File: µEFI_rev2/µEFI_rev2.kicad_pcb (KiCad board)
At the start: 4 copper layers, 99.9 x 99.3 mm, 149 parts, among them J1 USB_B, J2 Tag connect, J3 36638-0002, Q1 ISL9V5045S3ST, Q2 ISL9V5045S3ST, Q3 ISL9V5045S3ST, Q4 ISL9V5045S3ST, Q5 2N3904, Q6 IRF540N, Q7 IRF540N, Q8 SS8050, Q9 SS8050, SW1 SW_Push, U1 MCZ33810EK, U10 SensorsV2, U11 SensorsV2, U12 SensorsV2, U13 SensorsV2, U14 SensorsV2, U2 SensorsV2, U20 TPL7407LAPWR, U22 TPL7407LAPWR, U23 PaP_Driver_v1, U27 LM321, U3 STM32F407VGTx, U31 LM321, U36 MAX9926UAEE+, U4 MIC2940A-3.3WU, U5 MIC2940A-5.0WT, U6 LT4363IMS, U7 25LCxxx, U8 SensorsV2, U9 SensorsV2, Y1 25MHz

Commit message: uEFI v2 beta release
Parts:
- added C34: 4.7nF, Capacitor_SMD:C_0805_2012Metric, F.Cu at (125.2, 97.9)
- added H1: MountingHole, MountingHole:MountingHole_2.2mm_M2_Pad_Via, F.Cu at (99.9, 141.1)
- added H2: MountingHole, MountingHole:MountingHole_2.2mm_M2_Pad_Via, F.Cu at (188.9, 59.3)
- added H3: MountingHole, MountingHole:MountingHole_2.2mm_M2_Pad_Via, F.Cu at (130.3, 74.0)
- added H4: MountingHole, MountingHole:MountingHole_2.2mm_M2_Pad_Via, F.Cu at (186.9, 141.7)
- added H5: MountingHole, TestPoint:TestPoint_Pad_D1.0mm, F.Cu at (95.6, 145.0)
- added H6: MountingHole, TestPoint:TestPoint_Pad_D1.0mm, F.Cu at (190.1, 53.1)
- added H7: MountingHole, TestPoint:TestPoint_Pad_D1.0mm, F.Cu at (99.6, 53.0)
- added H8: MountingHole, TestPoint:TestPoint_Pad_D1.0mm, F.Cu at (158.7, 131.2)
- added Q10: IRF540N, Package_TO_SOT_THT:TO-220-3_Vertical, F.Cu at (183.0, 99.0)
- added R1: R_Small, Resistor_SMD:R_1206_3216Metric, F.Cu at (118.9, 98.3)
- added R28: R_Small, Resistor_SMD:R_1206_3216Metric, F.Cu at (121.4, 98.3)
- added R33: 10R 1/10W, Resistor_SMD:R_0603_1608Metric, B.Cu at (180.8, 100.1)
- added TP3: TestPoint, TestPoint:TestPoint_Pad_1.0x1.0mm, B.Cu at (126.2, 62.2)
- added TP4: TestPoint, TestPoint:TestPoint_Pad_1.0x1.0mm, B.Cu at (122.3, 82.8)
- added TP5: TestPoint, TestPoint:TestPoint_Pad_1.0x1.0mm, B.Cu at (120.2, 82.8)
- added TP6: TestPoint, TestPoint:TestPoint_Pad_1.0x1.0mm, B.Cu at (116.8, 64.8)
- added TP7: TestPoint, TestPoint:TestPoint_Pad_1.0x1.0mm, B.Cu at (120.4, 86.2)
- added TP8: TestPoint, TestPoint:TestPoint_Pad_1.0x1.0mm, B.Cu at (120.4, 89.6)
- added U15: TJA1042T3118, Package_SO:HTSOP-8-1EP_3.9x4.9mm_P1.27mm_EP2.4x3.2mm, F.Cu at (120.0, 105.2)
- C10, C11, C13, C15, C16, C19, C2, C21, C24, C26, C3, C5, C6, R10, R12, R14, R16: moved to B.Cu
- D2, D3: footprint Diode_SMD:D_0805_2012Metric -> Diode_SMD:D_SOD-523
- Q5: value 2N3904 -> SS8050; footprint Package_TO_SOT_SMD:TSOT-23 -> Package_TO_SOT_SMD:SOT-23
- moved JP11 164.7 mm to (175.9, 127.3)
- moved D14 162.6 mm to (174.8, 123.0)
- moved R82 158.7 mm to (171.0, 122.2), turned to 90 degrees
- moved C51 156.8 mm to (167.7, 126.7), turned to -90 degrees
- moved U27 154.3 mm to (172.1, 126.7)
- moved R83 152.9 mm to (167.7, 122.6), turned to 90 degrees
- moved C16 137.7 mm to (188.6, 117.0)
- moved R2 116.3 mm to (130.0, 118.6), turned to 90 degrees
- moved J2 105.9 mm to (142.8, 132.8), turned to 45 degrees
- moved TP1 99.0 mm to (128.5, 121.4)
- moved C11 97.2 mm to (123.0, 125.9), turned to -90 degrees
- moved C6 96.3 mm to (121.6, 143.8), turned to -45 degrees
- moved C12 92.6 mm to (137.2, 131.9), turned to 0 degrees
- moved C13 89.3 mm to (118.3, 131.7)
- moved C5 87.2 mm to (111.6, 136.4), turned to -135 degrees
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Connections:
- C18 pad 1: CONN_62 -> M1
- C19 pad 1: CONN_42 -> M2
- C20 pad 1: CONN_61 -> L1
- C21 pad 1: CONN_41 -> L2
- C23 pad 1: CONN_61 -> L1
- C24 pad 1: CONN_41 -> L2
- C25 pad 1: CONN_62 -> M1
- C26 pad 1: CONN_42 -> M2
- C27 pad 2: CONN_22 -> L4
- C28 pad 2: CONN_2 -> L3
- C29 pad 2: CONN_1 -> M4
- C30 pad 2: CONN_21 -> M3
- C49 pad 1: CONN_17 -> B1
- C52 pad 1: CONN_68 -> CMP-
- C53 pad 1: CONN_69 -> CMP+
- C55 pad 1: CONN71+ -> CKP+
- C56 pad 1: CONN71- -> CKP-
- J1 pad 1: unconnected-(J1-Pad1) -> /VBUS
- J1 pad 4: GND1 -> GND
- J1 pad 5: GND1 -> GND
- J3 pad A1: unconnected-(J3-PadA1) -> A1
- J3 pad A2: unconnected-(J3-PadA2) -> A2
- J3 pad A3: unconnected-(J3-PadA3) -> A3
- J3 pad A4: unconnected-(J3-PadA4) -> +12VA
- J3 pad B1: unconnected-(J3-PadB1) -> B1
- J3 pad B2: unconnected-(J3-PadB2) -> B2
- J3 pad B3: unconnected-(J3-PadB3) -> B3
- J3 pad B4: unconnected-(J3-PadB4) -> B4
- J3 pad C1: unconnected-(J3-PadC1) -> C1
- J3 pad C2: unconnected-(J3-PadC2) -> C2
- J3 pad C3: unconnected-(J3-PadC3) -> C3
- J3 pad C4: unconnected-(J3-PadC4) -> C4
- J3 pad D1: unconnected-(J3-PadD1) -> D1
- J3 pad D2: unconnected-(J3-PadD2) -> D2
- J3 pad D3: unconnected-(J3-PadD3) -> D3
- J3 pad D4: unconnected-(J3-PadD4) -> D4
- J3 pad E1: unconnected-(J3-PadE1) -> E1
- J3 pad E2: unconnected-(J3-PadE2) -> E2
- J3 pad E3: unconnected-(J3-PadE3) -> E3
- J3 pad E4: unconnected-(J3-PadE4) -> E4
- J3 pad F1: unconnected-(J3-PadF1) -> F1
- J3 pad F2: unconnected-(J3-PadF2) -> F2
- J3 pad F3: unconnected-(J3-PadF3) -> F3
- J3 pad F4: unconnected-(J3-PadF4) -> F4
- J3 pad G1: unconnected-(J3-PadG1) -> G1
- J3 pad G2: unconnected-(J3-PadG2) -> G2
- J3 pad G3: unconnected-(J3-PadG3) -> G3
- J3 pad G4: unconnected-(J3-PadG4) -> G4
- J3 pad H1: unconnected-(J3-PadH1) -> H1
- J3 pad H2: unconnected-(J3-PadH2) -> H2
- J3 pad H3: unconnected-(J3-PadH3) -> H3
- J3 pad H4: unconnected-(J3-PadH4) -> H4
- J3 pad J1: unconnected-(J3-PadJ1) -> J1
- J3 pad J2: unconnected-(J3-PadJ2) -> CAN+
- J3 pad J3: unconnected-(J3-PadJ3) -> CMP-
- J3 pad J4: unconnected-(J3-PadJ4) -> CKP-
- J3 pad K1: unconnected-(J3-PadK1) -> K1
- J3 pad K2: unconnected-(J3-PadK2) -> CAN-
- J3 pad K3: unconnected-(J3-PadK3) -> CMP+
- J3 pad K4: unconnected-(J3-PadK4) -> CKP+
- J3 pad L1: unconnected-(J3-PadL1) -> L1
- J3 pad L2: unconnected-(J3-PadL2) -> L2
- J3 pad L3: unconnected-(J3-PadL3) -> L3
- J3 pad L4: unconnected-(J3-PadL4) -> L4
- J3 pad M1: unconnected-(J3-PadM1) -> M1
- J3 pad M2: unconnected-(J3-PadM2) -> M2
- J3 pad M3: unconnected-(J3-PadM3) -> M3
- J3 pad M4: unconnected-(J3-PadM4) -> M4
- Q1 pad 2: CONN_42 -> M2
- Q2 pad 2: CONN_62 -> M1
- Q3 pad 2: CONN_61 -> L1
- Q4 pad 2: CONN_41 -> L2
- Q5 pad 1: +12VA -> Net-(D2-Pad1)
- Q5 pad 2: Net-(D2-Pad1) -> +12VA
- R112 pad 1: CONN_68 -> CMP-
- R116 pad 1: CONN71- -> CKP-
- R117 pad 1: CONN71+ -> CKP+
- R13 pad 2: CONN_62 -> M1
- R14 pad 2: CONN_42 -> M2
- R15 pad 2: CONN_61 -> L1
- R16 pad 2: CONN_41 -> L2
- R24 pad 2: /CAN_RX -> /LED_CAN_RX
- R5 pad 2: /CAN_TX -> /LED_CAN_TX
- R81 pad 1: CONN_69 -> CMP+
- R87 pad 1: CONN_17 -> B1
- R92 pad 1: CONN_17 -> B1
- R97 pad 2: CONN_17 -> B1
- U1 pad 1: CONN_21 -> M3
- U1 pad 16: CONN_1 -> M4
- U1 pad 17: CONN_22 -> L4
- U1 pad 32: CONN_2 -> L3
- U10 pad 1: unconnected-(U10-Pad1) -> +5VA
- U10 pad 2: unconnected-(U10-Pad2) -> +12V
- U10 pad 3: unconnected-(U10-Pad3) -> J1
- U10 pad 4: unconnected-(U10-Pad4) -> /Sensores/PA3
- U10 pad 5: unconnected-(U10-Pad5) -> GND
- U11 pad 1: unconnected-(U11-Pad1) -> +5VA
- U11 pad 2: unconnected-(U11-Pad2) -> +12V
- U11 pad 3: unconnected-(U11-Pad3) -> D1
- U11 pad 4: unconnected-(U11-Pad4) -> /Sensores/PA4
- U11 pad 5: unconnected-(U11-Pad5) -> GND
- U12 pad 1: unconnected-(U12-Pad1) -> +5VA
- U12 pad 2: unconnected-(U12-Pad2) -> +12V
- U12 pad 3: unconnected-(U12-Pad3) -> F1
- U12 pad 4: unconnected-(U12-Pad4) -> /Sensores/PA5
- U12 pad 5: unconnected-(U12-Pad5) -> GND
- U13 pad 1: unconnected-(U13-Pad1) -> +5VA
- U13 pad 2: unconnected-(U13-Pad2) -> +12V
- U13 pad 3: unconnected-(U13-Pad3) -> C1
- U13 pad 4: unconnected-(U13-Pad4) -> /Sensores/PA6
- U13 pad 5: unconnected-(U13-Pad5) -> GND
- U14 pad 1: unconnected-(U14-Pad1) -> +5VA
- U14 pad 2: unconnected-(U14-Pad2) -> +12V
- U14 pad 3: unconnected-(U14-Pad3) -> G1
- U14 pad 4: unconnected-(U14-Pad4) -> /Sensores/PA7
- U14 pad 5: unconnected-(U14-Pad5) -> GND
- U2 pad 1: unconnected-(U2-Pad1) -> +5VA
- U2 pad 2: unconnected-(U2-Pad2) -> +12V
- U2 pad 3: unconnected-(U2-Pad3) -> K1
- U2 pad 4: unconnected-(U2-Pad4) -> /Sensores/PA0
- U2 pad 5: unconnected-(U2-Pad5) -> GND
- U20 pad 10: CONN_58 -> D3
- U20 pad 11: CONN_18 -> E3
- U20 pad 12: CONN_39 -> B4
- U20 pad 13: CONN_39 -> B4
- U20 pad 14: CONN_40 -> C4
- U20 pad 15: CONN_40 -> C4
- U20 pad 16: CONN_40 -> C4
- U22 pad 10: CONN_63 -> F3
- U22 pad 11: CONN_64 -> D4
- U22 pad 12: CONN_64 -> D4
- U22 pad 13: CONN_65 -> G3
- U22 pad 14: CONN_65 -> G3
- U22 pad 15: CONN_66 -> H3
- U22 pad 16: CONN_66 -> H3
- U22 pad 7: /PWM/Relays/R3 -> /R_LMB
- U23 pad 11: CONN_75 -> H4
- U23 pad 12: CONN_76 -> G4
- U23 pad 13: CONN_77 -> F4
- U23 pad 14: CONN_78 -> E4
- U3 pad 15: unconnected-(U3-Pad15) -> 5V_ENABLE
- U8 pad 1: unconnected-(U8-Pad1) -> +5VA
- U8 pad 2: unconnected-(U8-Pad2) -> +12V
- U8 pad 3: unconnected-(U8-Pad3) -> E1
- U8 pad 4: unconnected-(U8-Pad4) -> /Sensores/PA1
- U8 pad 5: unconnected-(U8-Pad5) -> GND
- U9 pad 1: unconnected-(U9-Pad1) -> +5VA
- U9 pad 2: unconnected-(U9-Pad2) -> +12V
- U9 pad 3: unconnected-(U9-Pad3) -> H1
- U9 pad 4: unconnected-(U9-Pad4) -> /Sensores/PA2
- U9 pad 5: unconnected-(U9-Pad5) -> GND
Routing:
- net +3V3: track 0.00 -> 265.6 mm, vias 0 -> 15
- net +12V: track 0.00 -> 253.3 mm, vias 1 -> 4
- net GND: track 17.4 -> 191.6 mm, vias 11 -> 53
- net /MIL_OUT: track 0.00 -> 170.0 mm, vias 0 -> 6
- net /CHK_OUT: track 0.00 -> 164.2 mm, vias 0 -> 4
- net +5VA: track 15.5 -> 127.5 mm, vias 3 -> 4
- net /VBUS: track 0.00 -> 104.3 mm, vias 0 -> 2
- net /Sensores/PA7: track 0.00 -> 98.2 mm, vias 0 -> 2
- net /TIM9_CH2: track 0.00 -> 97.2 mm, vias 0 -> 2
- net /TIM9_CH1: track 0.00 -> 96.5 mm, vias 0 -> 2
- net 5V_ENABLE: track 0.00 -> 94.6 mm, vias 0 -> 2
- net /Sensores/PA6: track 0.00 -> 94.0 mm, vias 0 -> 1
- net /MTR_ENABLE: track 0.00 -> 89.8 mm, vias 0 -> 1
- net /R_LMB: track 0.00 -> 89.5 mm, vias 0 -> 2
- net /Sensores/PA3: track 0.00 -> 87.3 mm, vias 0 -> 1
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- added copper zone on B.Cu, net +3V3
- added copper zone on F.Cu, net +3V3
- added copper zone on B.Cu, net GND
- added copper zone on F.Cu, net GND
- added copper zone on In2.Cu, net GND
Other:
- board text added: "Aca podria ir otro soporte, pero de plastico, tipo trabita"
- board text added: "Aca va a ir un header con todos los pines que esten al pedo y sirvan para hacer de expansora"
- board text added: "Alimentacion sensores:"
- board text added: "Battery"
- board text added: "EN"
- board text added: "Faltan los caps elec[..] para filtrar el ruido, tambien ceramicos / tantalio"
- board text added: "Flash"
- board text added: "O2 Sensor"
- board text added: "PaP Driver"
- board text added: "RESET"
- board text added: "Salida tacometro"
- board text removed: "GNC_IN"
- board text removed: "O2 Sensor (A)"
- board text removed: "RPM_OUT"
- board text removed: "RSP ?"
- board text removed: "can"
- board text removed: "ckp"
- board text removed: "cmp"

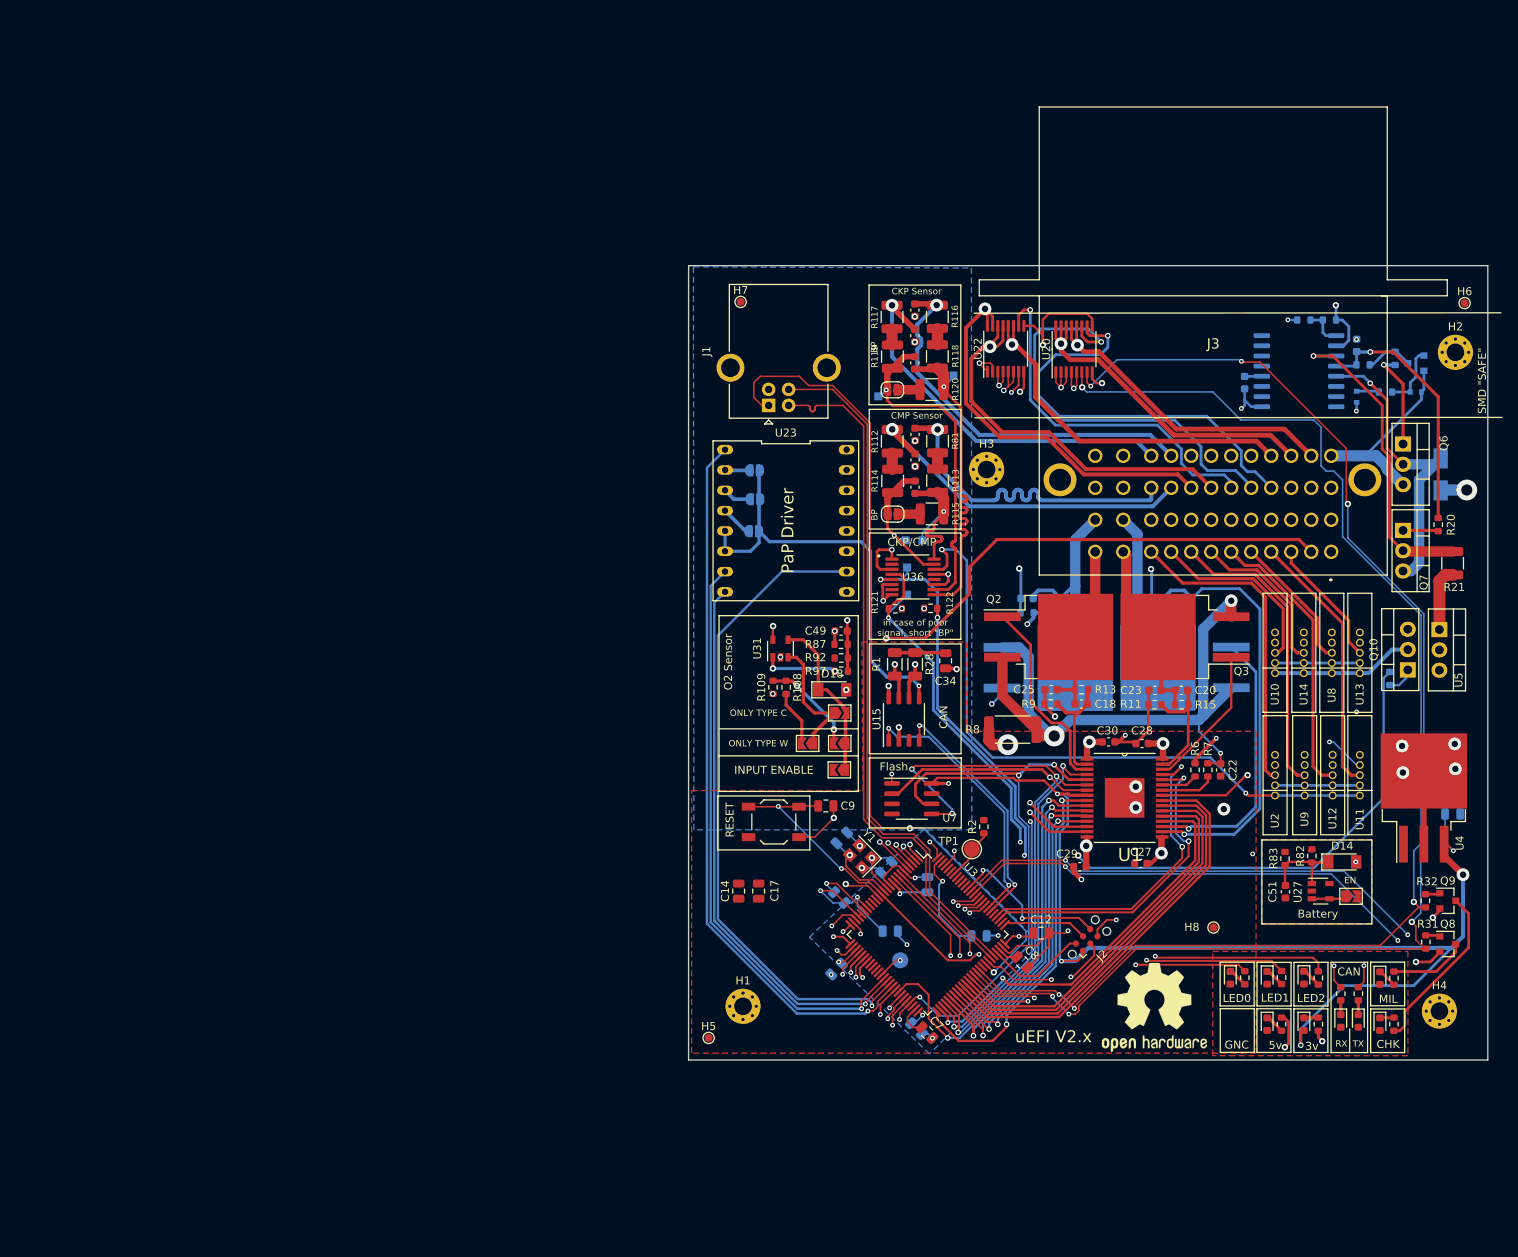
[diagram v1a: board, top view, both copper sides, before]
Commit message: bump to kicad 6, init uEFI v3
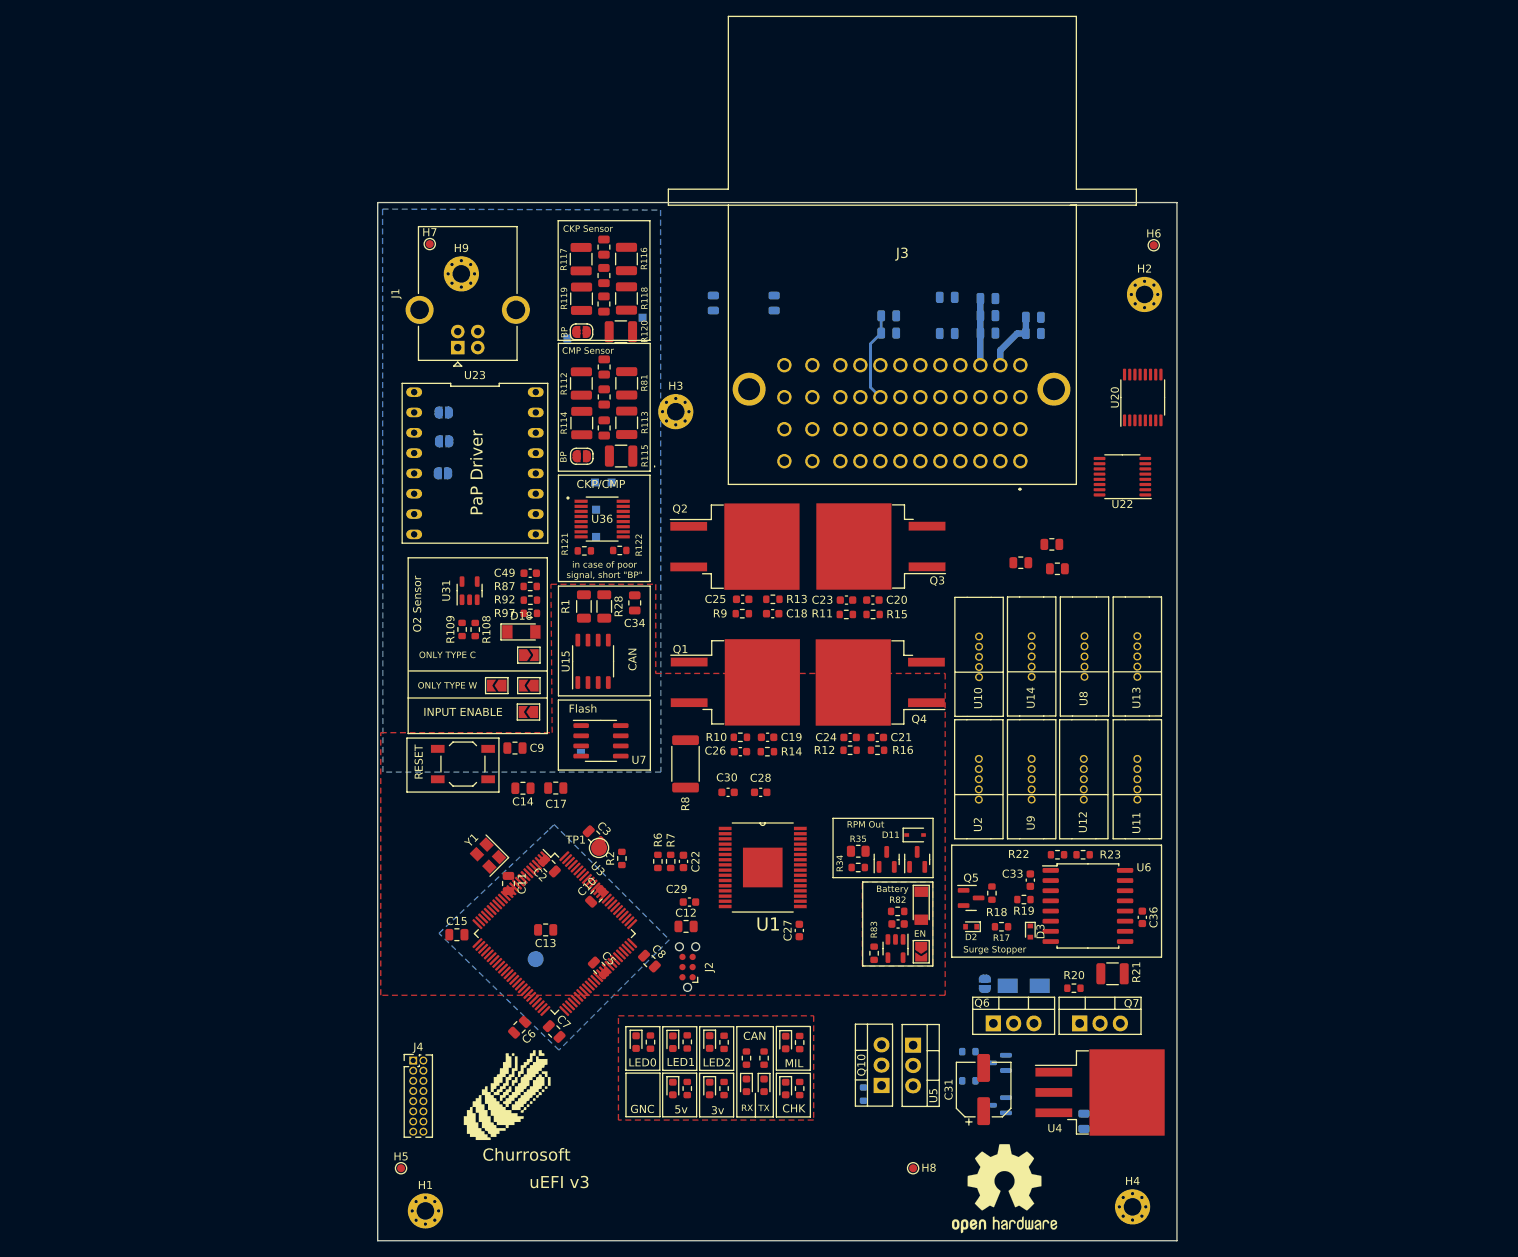
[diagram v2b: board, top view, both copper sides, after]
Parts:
- added C31: 100uF ±20% 35V, Capacitor_SMD:CP_Elec_6.3x7.7, F.Cu at (130.0, 151.5)
- added Churrosoft: SYM_Hot_Large, OpenEFI-STM32F_rev3:churro_new_v4, F.Cu at (70.6, 152.1)
- added D11: MM3Z24VT1G, Diode_SMD:D_SOD-323, F.Cu at (121.4, 119.6)
- added F1: 750mA, Fuse:Fuse_0805_2012Metric, B.Cu at (118.1, 54.7)
- added F10: 750mA, Fuse:Fuse_0805_2012Metric, B.Cu at (136.2, 54.9)
- added F11: 750mA, Fuse:Fuse_0805_2012Metric, B.Cu at (136.2, 56.9)
- added F12: 750mA, Fuse:Fuse_0805_2012Metric, F.Cu at (134.6, 85.6)
- added F13: 750mA, Fuse:Fuse_0805_2012Metric, B.Cu at (125.4, 52.4)
- added F14: 750mA, Fuse:Fuse_0805_2012Metric, B.Cu at (125.4, 56.9)
- added F2: 750mA, Fuse:Fuse_0805_2012Metric, F.Cu at (139.2, 86.4)
- added F3: 750mA, Fuse:Fuse_0805_2012Metric, B.Cu at (118.1, 56.9)
- added F4: 750mA, Fuse:Fuse_0805_2012Metric, B.Cu at (103.8, 53.1)
- added F5: 750mA, Fuse:Fuse_0805_2012Metric, B.Cu at (130.5, 56.9)
- added F6: 750mA, Fuse:Fuse_0805_2012Metric, B.Cu at (96.2, 53.1)
- added F7: 750mA, Fuse:Fuse_0805_2012Metric, B.Cu at (130.5, 54.7)
- added F8: 750mA, Fuse:Fuse_0805_2012Metric, B.Cu at (130.5, 52.6)
- added F9: 750mA, Fuse:Fuse_0805_2012Metric, F.Cu at (138.5, 83.3)
- added H9: MountingHole, MountingHole:MountingHole_2.2mm_M2_Pad_Via, F.Cu at (64.7, 49.5)
- added J4: Conn_02x08_Odd_Even, Connector_PinHeader_1.27mm:PinHeader_2x08_P1.27mm_Vertical, F.Cu at (58.7, 147.8)
- added JP4: Jumper_NO_Small, Jumper:SolderJumper-2_P1.3mm_Open_RoundedPad1.0x1.5mm, B.Cu at (130.1, 138.2)
- added Q11: SS8050, Package_TO_SOT_SMD:SOT-23, F.Cu at (117.9, 122.7)
- added Q12: AO3400A, Package_TO_SOT_SMD:SOT-23, F.Cu at (121.7, 122.7)
- added R34: 1k, Resistor_SMD:R_0603_1608Metric, F.Cu at (114.3, 123.7)
- added R35: 100k, Resistor_SMD:R_0805_2012Metric, F.Cu at (114.3, 121.7)
- added TP9: TestPoint, TestPoint:TestPoint_Pad_1.0x1.0mm, B.Cu at (79.6, 109.4)
- C10, C11, C13, C15, C19, C2, C21, C24, C26, C3, C33, C36, C5, C6, D2, D3, Q1, Q4, Q5, R10, R12, R14, R16, R17, R18, R19, R22, R23, U6: moved to F.Cu
- C52, C53, C54, C55, C56, C57: footprint Capacitor_SMD:C_0603_1608Metric -> Capacitor_SMD:C_0805_2012Metric
- Q8, Q9, R31, R32: moved to B.Cu
- R24, R25, R26, R27, R29, R3, R30, R4, R5: value R_Small -> 4.7k
- moved Q6 88.7 mm to (131.2, 143.2), turned to 0 degrees
- moved D2 86.9 mm to (128.4, 131.1), turned to 180 degrees
- moved Q5 86.9 mm to (128.4, 127.5), turned to 0 degrees
- moved Q10 83.8 mm to (117.2, 150.9)
- moved R33 83.8 mm to (115.0, 152.0)
- moved U5 83.8 mm to (121.2, 145.9)
- moved R18 83.7 mm to (131.0, 126.9)
- moved D4 82.5 mm to (135.0, 138.5), turned to 0 degrees
- moved R17 82.3 mm to (132.2, 131.1), turned to 0 degrees
- moved R19 79.2 mm to (135.0, 127.7), turned to 180 degrees
- moved D3 78.3 mm to (135.8, 131.7)
- moved C33 78.3 mm to (135.8, 125.3)
- moved R22 75.0 mm to (139.2, 122.1), turned to 0 degrees
- moved D7 74.7 mm to (100.3, 150.9)
- moved R24 74.7 mm to (100.3, 147.5)
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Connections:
- J3 pad A2: A2 -> +5VA
- J3 pad A3: A3 -> GND
- J3 pad B2: B2 -> +5VA
- J3 pad B3: B3 -> GND
- J3 pad C2: C2 -> +5VA
- J3 pad C3: C3 -> GND
- J3 pad D2: D2 -> +5VA
- J3 pad E2: E2 -> +5VA
- J3 pad F2: F2 -> +5VA
- J3 pad G2: G2 -> GND
- J3 pad H2: H2 -> GND
- J3 pad MH1: unconnected-(J3-PadMH1) -> GND
- J3 pad MH2: unconnected-(J3-PadMH2) -> GND
- U20 pad 10: D3 -> /PWM/Relays/MIL_OUT
- U20 pad 11: E3 -> /PWM/Relays/CHECK_ENGINE
- U20 pad 12: B4 -> Net-(U20-Pad12)
- U20 pad 13: B4 -> Net-(U20-Pad13)
- U20 pad 14: C4 -> Net-(U20-Pad14)
- U20 pad 15: C4 -> Net-(U20-Pad15)
- U20 pad 16: C4 -> Net-(U20-Pad16)
- U22 pad 10: F3 -> /PWM/Relays/R3_OUT
- U22 pad 11: D4 -> Net-(U22-Pad11)
- U22 pad 12: D4 -> Net-(U22-Pad12)
- U22 pad 13: G3 -> Net-(U22-Pad13)
- U22 pad 14: G3 -> Net-(U22-Pad14)
- U22 pad 15: H3 -> Net-(U22-Pad15)
- U22 pad 16: H3 -> Net-(U22-Pad16)
- U3 pad 15: 5V_ENABLE -> /Sensores/PC0
- U3 pad 16: unconnected-(U3-Pad16) -> 5V_ENABLE
- U3 pad 18: unconnected-(U3-Pad18) -> /AUX_OUT_2
- U3 pad 33: unconnected-(U3-Pad33) -> /AUX_OUT_1
- U3 pad 34: unconnected-(U3-Pad34) -> /Sensores/PC5
- U3 pad 35: unconnected-(U3-Pad35) -> /AUX_OUT_3
- U3 pad 91: /MTR_M_2 -> unconnected-(U3-Pad91)
- U3 pad 92: /MTR_M1 -> unconnected-(U3-Pad92)
- U3 pad 93: /PAP_ENABLE -> unconnected-(U3-Pad93)
- U3 pad 95: /PWM_ENABLE_2 -> unconnected-(U3-Pad95)
- U3 pad 96: /PWM_ENABLE_1 -> unconnected-(U3-Pad96)
- U7 pad 3: unconnected-(U7-Pad3) -> +3V3
- U7 pad 7: unconnected-(U7-Pad7) -> +3V3
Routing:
- net +3V3: track 265.6 -> 0.00 mm, vias 15 -> 0
- net +12V: track 253.3 -> 0.00 mm, vias 4 -> 0
- net GND: track 191.6 -> 0.00 mm, vias 53 -> 0
- net /MIL_OUT: track 170.0 -> 0.00 mm, vias 6 -> 0
- net /CHK_OUT: track 164.2 -> 0.00 mm, vias 4 -> 0
- net +5VA: track 127.5 -> 0.00 mm, vias 4 -> 0
- net /VBUS: track 104.3 -> 0.00 mm, vias 2 -> 0
- net /Sensores/PA7: track 98.2 -> 0.00 mm, vias 2 -> 0
- net /TIM9_CH2: track 97.2 -> 0.00 mm, vias 2 -> 0
- net /TIM9_CH1: track 96.5 -> 0.00 mm, vias 2 -> 0
- net 5V_ENABLE: track 94.6 -> 0.00 mm, vias 2 -> 0
- net /Sensores/PA6: track 94.0 -> 0.00 mm, vias 1 -> 0
- net /MTR_ENABLE: track 89.8 -> 0.00 mm, vias 1 -> 0
- net /R_LMB: track 89.5 -> 0.00 mm, vias 2 -> 0
- net /Sensores/PA3: track 87.3 -> 0.00 mm, vias 1 -> 0
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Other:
- board size 99.9 x 99.3 mm -> 99.9 x 129.8 mm
- board text added: "De aca puedo sacar 12v para detectar ACC"
- board text added: "Esta parte del conector tiene que quedar afuera del pcb:"
- board text added: "JLCJLCJLCJLC"
- board text added: "Lote:"
- board text added: "Mover"
- board text added: "Notes:"
- board text added: "PWM0"
- board text added: "PWM1"
- board text added: "RPM Out"
- board text added: "Rev:"
- board text added: "uEFI v3"
- board text removed: "Aca podria ir otro soporte, pero de plastico, tipo trabita"
- board text removed: "Aca va a ir un header con todos los pines que esten al pedo y sirvan para hacer de expansora"
- board text removed: "Alimentacion sensores:"
- board text removed: "Faltan los caps elec[..] para filtrar el ruido, tambien ceramicos / tantalio"
- board text removed: "SMD {dblquote}SAFE{dblquote}"
- board text removed: "Salida tacometro"
- board text removed: "uEFI V2.x"
